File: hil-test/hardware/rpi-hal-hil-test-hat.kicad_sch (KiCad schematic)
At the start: 6 parts, among them J1 GPIO, U1 CAT24C256

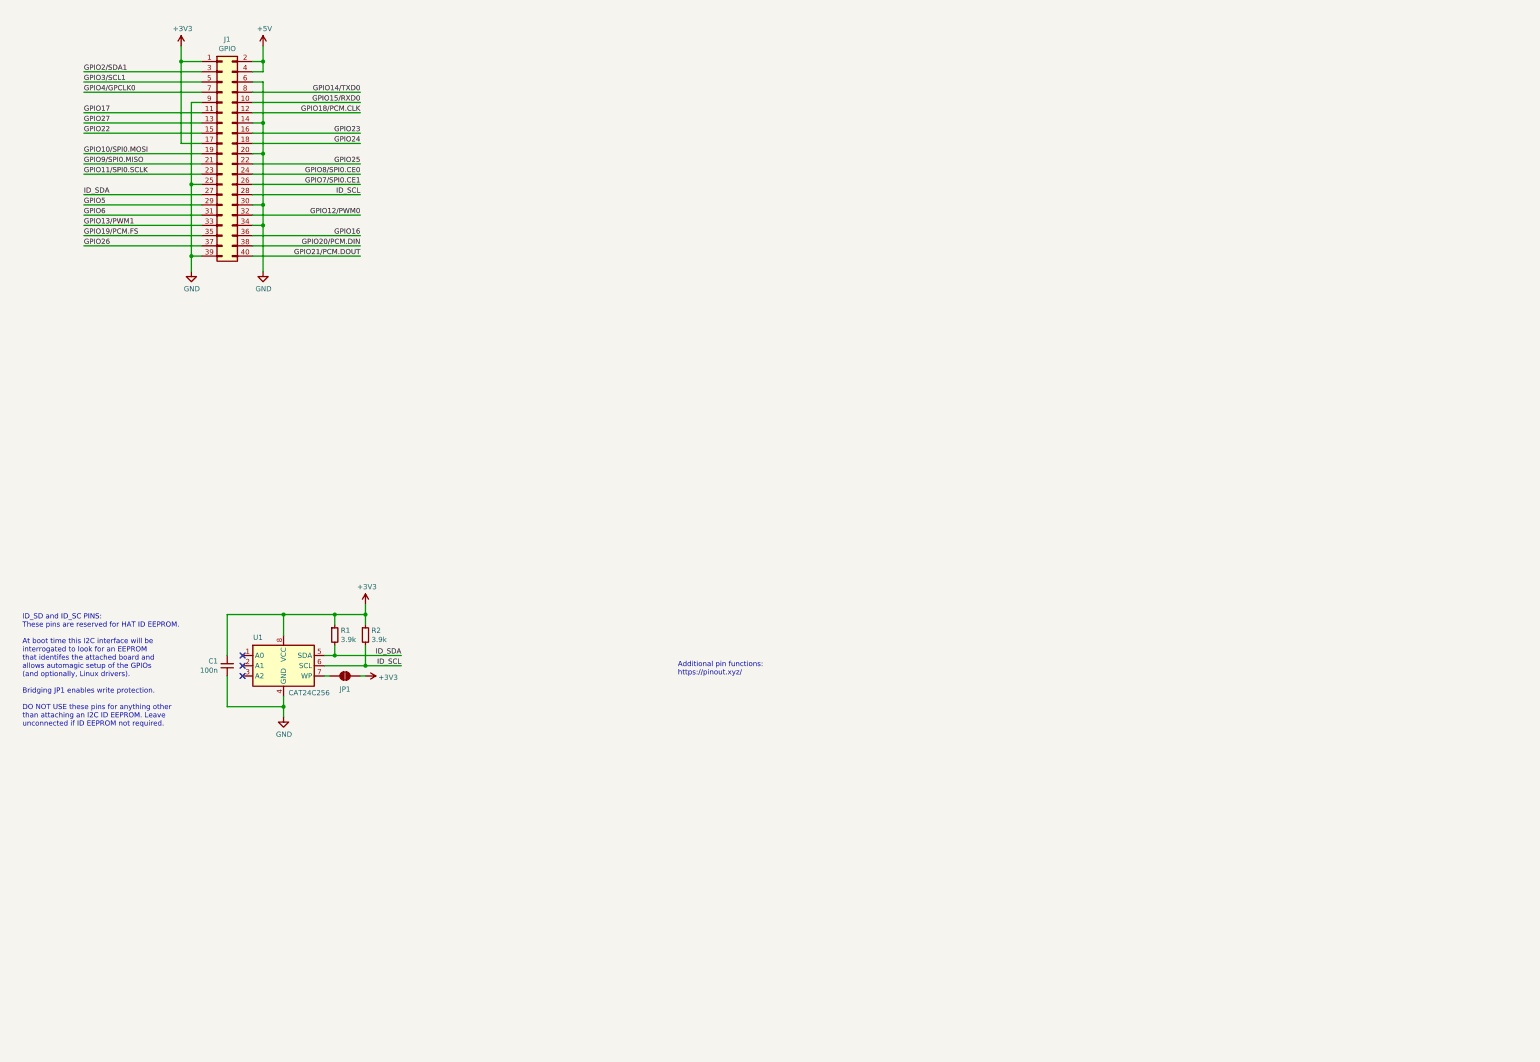
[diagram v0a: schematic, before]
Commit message: pico schematic symbol
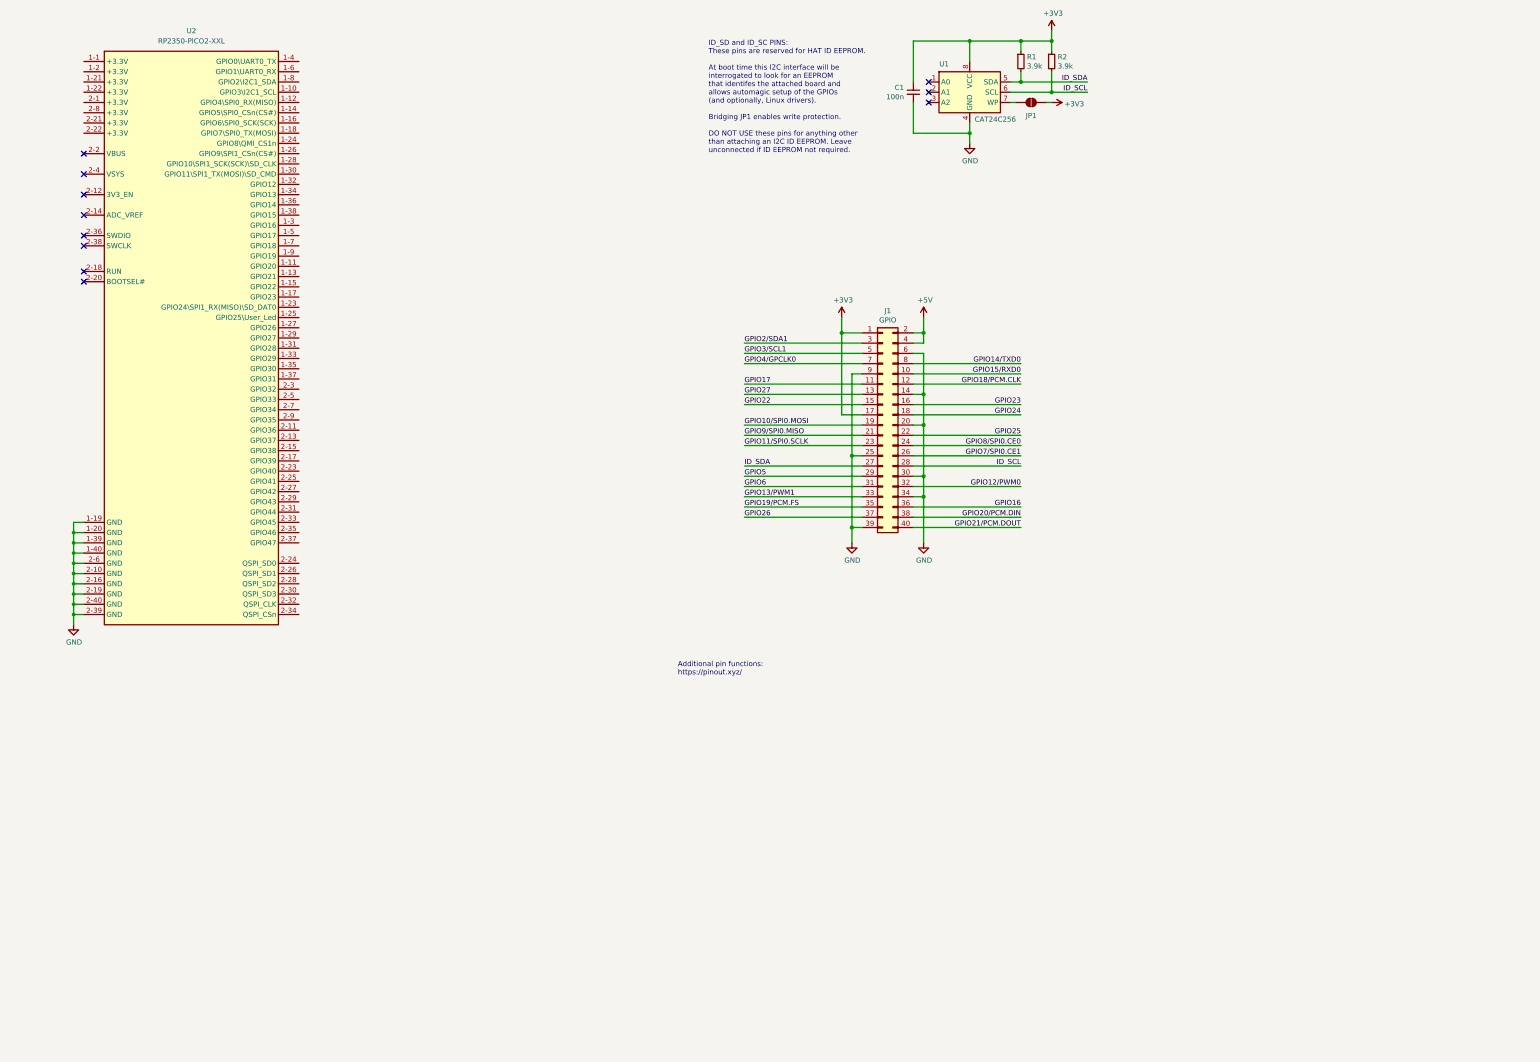
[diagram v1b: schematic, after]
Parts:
- added U2: RP2350-PICO2-XXL, symbol rpi-hal-hil-test-hat:RP2350-PICO2-XXL
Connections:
- net GND: now also U2.1-19 (GND), U2.1-20 (GND), U2.1-39 (GND), U2.1-40 (GND), U2.2-10 (GND), U2.2-16 (GND), U2.2-19 (GND), U2.2-39 (GND), U2.2-40 (GND), U2.2-6 (GND)
- no-connect marks 3 -> 11
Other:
- moved on the sheet: C1, J1, JP1, R1, R2, U1

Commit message: wip
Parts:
- added R10, R12, R4: 10k, symbol Device:R_Small
- added R11, R3, R5, R6, R7, R8, R9: 1k, symbol Device:R_Small
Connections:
- net GND: now also R10.1, R12.1, R4.1
- net GPIO2/SDA1: now also R5.2
- net GPIO3/SCL1: now also R6.2
- net GPIO4/GPCLK0: now also R3.2
- net GPIO5: now also R9.2
- net GPIO6: now also R11.2
- net ID_SCL: now also R8.2
- net ID_SDA: now also R7.2
- net at U2.1-11 (GPIO20): now also R11.1, R12.2
- net at U2.1-3 (GPIO16): now also R7.1
- net at U2.1-36 (GPIO14): now also R5.1
- net at U2.1-38 (GPIO15): now also R6.1
- net at U2.1-5 (GPIO17): now also R8.1
- net at U2.1-7 (GPIO18): now also R3.1, R4.2
- net at U2.1-9 (GPIO19): now also R10.2, R9.1

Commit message: wip
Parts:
- added C1: 1uF, symbol Device:C_Small
- added J1: POWER, symbol Connector_Generic:Conn_01x02
- added J2: PI.POWER, symbol Connector_Generic:Conn_01x02
- added J3: AudioJack3, symbol Connector_Audio:AudioJack3
- added R10: 10m, symbol Device:R_Small
- added R11, R12, R13, R14, R15, R16, R17, R18, R19, R20, R21, R22, R23, R24, R25, R4, R5, R6, R7, R8, R9: 8.2k, symbol Device:R_Small
- added R26, R27, R35, R36, R37, R38, R39, R40, R41, R42, R43, R44, R45, R46, R47, R48, R49, R50, R51, R52, R53: 1k, symbol Device:R_Small
- added U2: TPS22958x, symbol rpi-hal-hil-test-hat:TPS22958x
- added U3: INA226, Package_SO:TSSOP-10_3x3mm_P0.5mm, symbol Sensor_Energy:INA226
- J4: renamed from J1; value GPIO -> PI
- R1: renamed from R4; value 10k -> 8.2k
- R2: renamed from R10; value 10k -> 8.2k
- R3: renamed from R12; value 10k -> 8.2k
- renumbered C1 to C2, R5 to R28, R6 to R29, R7 to R30, R8 to R31, R3 to R32, R9 to R33, R11 to R34, R1 to R54, R2 to R55, U2 to U1, U1 to U4
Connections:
- net +3V3 is gone; now on net PI3V3: C2.1, J4.1 (Pin_1), J4.17 (Pin_17), JP1.2 (B), R54.1, R55.1, U4.8 (VCC)
- net GND: now also C1.2, J1.2 (Pin_2), J3.S, R10.2, R11.1, R12.1, R13.1, R14.1, R15.1, R16.1, R17.1, R18.1, R19.1, R20.1, R21.1, R22.1, R23.1, R24.1, R25.1, R4.1, R5.1, R6.1, R7.1, R8.1, R9.1, U2.6 (GND), U3.1 (A1), U3.2 (A0), U3.7 (GND), U3.9 (Vin-)
- net GPIO10/SPI0.MOSI: now also R38.2
- net GPIO11/SPI0.SCLK: now also R39.2
- net GPIO12/PWM0: now also R40.2
- net GPIO13/PWM1: now also R41.2
- net GPIO14/TXD0: now also R27.2
- net GPIO15/RXD0: now also R26.2
- net GPIO16: now also R42.2
- net GPIO17: now also R43.2
- net GPIO18/PCM.CLK: now also R44.2
- net GPIO19/PCM.FS: now also R45.2
- net GPIO20/PCM.DIN: now also R46.2
- net GPIO21/PCM.DOUT: now also R47.2
- net GPIO22: now also R48.2
- net GPIO23: now also R49.2
- net GPIO24: now also R50.2
- net GPIO25: now also R51.2
- net GPIO26: now also R52.2
- net GPIO27: now also R53.2
- net GPIO7/SPI0.CE1: now also R35.2
- net GPIO8/SPI0.CE0: now also R36.2
- net GPIO9/SPI0.MISO: now also R37.2
- net +3.3V: now reaches U1.1-1 (+3.3V)
- net +3.3V: now also U3.6 (VS)
- net INA226.SDA: now reaches U1.1-12 (GPIO4\SPI0_RX(MISO))
- net INA226.SDA: now also U3.4 (SDA)
- net at U1.1-13 (GPIO21): now also R35.1, R4.2
- net INA226.SCL: now reaches U1.1-14 (GPIO5\SPI0_CSn(CS#))
- net INA226.SCL: now also U3.5 (SCL)
- net at U1.1-15 (GPIO22): now also R36.1, R5.2
- net at U1.1-17 (GPIO23): now also R37.1, R6.2
- net at U1.1-27 (GPIO26): now also R38.1, R7.2
- net at U1.1-29 (GPIO27): now also R39.1, R8.2
- net at U1.1-31 (GPIO28): now also R40.1, R9.2
- net at U1.1-32 (GPIO12): now also R12.2, R26.1
- net at U1.1-33 (GPIO29): now also R11.2, R41.1
- net at U1.1-34 (GPIO13): now also R13.2, R27.1
- net at U1.1-35 (GPIO30): now also R14.2, R42.1
- net at U1.1-37 (GPIO31): now also R15.2, R43.1
- net PWR_EN: now reaches U1.1-4 (GPIO0\UART0_TX)
- net PWR_EN: now also U2.2 (ON)
- net INA226.ALERT: now reaches U1.1-6 (GPIO1\UART0_RX)
- net INA226.ALERT: now also U3.3 (~{Alert})
- net at U1.2-11 (GPIO36): now also R20.2, R48.1
- net at U1.2-13 (GPIO37): now also R21.2, R49.1
- net at U1.2-15 (GPIO38): now also R22.2, R50.1
- net at U1.2-17 (GPIO39): now also R23.2, R51.1
- net at U1.2-23 (GPIO40): now also R24.2, R52.1
- net at U1.2-25 (GPIO41): now also R25.2, R53.1
- net AUDIO_L: now reaches U1.2-27 (GPIO42)
- net AUDIO_L: now also J3.T
- net AUDIO_R: now reaches U1.2-29 (GPIO43)
- net AUDIO_R: now also J3.R
- net at U1.2-3 (GPIO32): now also R16.2, R44.1
- net PI3V3: now reaches U1.2-31 (GPIO44)
- net at U1.2-5 (GPIO33): now also R17.2, R45.1
- net at U1.2-7 (GPIO34): now also R18.2, R46.1
- net at U1.2-9 (GPIO35): now also R19.2, R47.1
- net +5V: no longer names the net of J4.2 (Pin_2)
- net +5V: no longer J4.4 (Pin_4)
- new net: J2.2 (Pin_2), R10.1, U3.10 (Vin+), U3.8 (Vbus)
- new net: J1.1 (Pin_1), U2.1 (VIN), U2.3 (VBIAS)
- new net: C1.1, U2.7 (CT)
- new net: J2.1 (Pin_1), U2.5 (VOUT), U2.8 (VOUT)
- no-connect marks 11 -> 40
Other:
- note added: "Target Address: 1000000 (x40)"
- note removed: "Additional pin functions: https://pinout.xyz/"
- moved on the sheet: C2, J4, JP1, R1, R2, R28, R29, R3, R30, R31, R32, R33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

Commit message: wip
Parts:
- removed J3: AudioJack3, symbol Connector_Audio:AudioJack3
- added J3: MISC, symbol Connector_Generic:Conn_02x08_Odd_Even
- added J5: PI.POWER.DIRECT, symbol Connector_Generic:Conn_01x02
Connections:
- net +3.3V: now also J3.2 (Pin_2)
- net AUDIO_L: now also J3.4 (Pin_4)
- net AUDIO_R: now also J3.6 (Pin_6)
- net GND: now also J2.2 (Pin_2), J3.15 (Pin_15), J3.16 (Pin_16); no longer R10.2, U3.9 (Vin-)
- net PI5V: now reaches J4.2 (Pin_2)
- net PI5V: now also J4.4 (Pin_4), J5.2 (Pin_2)
- net at R10.1, U3.10 (Vin+), U3.8 (Vbus): now also U2.5 (VOUT), U2.8 (VOUT); no longer J2.2 (Pin_2)
- net VBUS1_EN: now reaches U1.1-16 (GPIO6\SPI0_SCK(SCK))
- net VBUS1_EN: now also J3.3 (Pin_3)
- net VBUS2_EN: now reaches U1.1-18 (GPIO7\SPI0_TX(MOSI))
- net VBUS2_EN: now also J3.7 (Pin_7)
- net VBUS3_EN: now reaches U1.1-25 (GPIO25\User_Led)
- net VBUS3_EN: now also J3.11 (Pin_11)
- net RUN_DRV: now reaches U1.1-8 (GPIO2\I2C1_SDA)
- net RUN_DRV: now also J3.1 (Pin_1)
- net VBUS1_FAULT: now reaches U1.2-33 (GPIO45)
- net VBUS1_FAULT: now also J3.5 (Pin_5)
- net VBUS2_FAULT: now reaches U1.2-35 (GPIO46)
- net VBUS2_FAULT: now also J3.9 (Pin_9)
- net VBUS3_FAULT: now reaches U1.2-37 (GPIO47)
- net VBUS3_FAULT: now also J3.13 (Pin_13)
- new net: J2.1 (Pin_1), J5.1 (Pin_1), R10.2, U3.9 (Vin-)
- no-connect marks 40 -> 34
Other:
- note added: "WARNING: This pin out matches the PI closely but should not be directly connected. This should be connected to a PI breakout board."
- moved on the sheet: J2, J4, R10, U3

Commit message: wip
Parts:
- added C3: 100nF, symbol Device:C_Small
- added R56, R57: 4.7k, symbol Device:R_Small
- added R58: 10k, symbol Device:R_Small
- C1: value 1uF -> 3.9nF
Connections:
- net +3.3V: now also R56.2, R57.2, R58.1
- net GND: now also U4.1 (A0), U4.2 (A1), U4.3 (A2), C3.2
- net INA226.ALERT: now also R58.2
- net at J1.1 (Pin_1), U2.1 (VIN), U2.3 (VBIAS): now also U2.4 (VIN), C3.1
- net at R30.1, U1.1-3 (GPIO16): now also R56.1
- net at R31.1, U1.1-5 (GPIO17): now also R57.1
- no-connect marks 34 -> 31
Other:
- moved on the sheet: C2
